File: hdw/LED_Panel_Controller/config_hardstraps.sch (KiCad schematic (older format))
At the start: 0 parts

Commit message: lots of schematic progress
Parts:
- added R? (x2): 10k, Resistors_SMD:R_0402, symbol Custom_Library:R_Custom
- added R? (x2): 10, Resistors_SMD:R_0402, symbol Custom_Library:R_Custom
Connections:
- new net +3V3: R?.1, R?.1
- new net GND: R?.2, R?.2
- new net ~ETC_Config: R?.1, R?.2
- new net ~Telemetry_Config: R?.1, R?.2
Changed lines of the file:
@@
 encoding utf-8
 Sheet 12 34
-Title ""
-Date "2020-09-08"
-Rev ""
-Comp ""
+Title "LED Panel Controller"
+Date "2020-12-23"
+Rev "A"
+Comp "Drew Maatman, Logan Wedel"
 Comment1 ""
 Comment2 ""
@@
 Comment4 ""
 $EndDescr
+$Comp
+L Custom_Library:R_Custom R?
+U 1 1 5FFD2F97
+P 2880 2230
+AR Path="/5D6B2673/5FFD2F97" Ref="R?"  Part="1"
+AR Path="/5D6C0D23/5FFD2F97" Ref="R?"  Part="1"
+AR Path="/5D77A516/5FFD2F97" Ref="R?"  Part="1"
+AR Path="/5E939CFF/5FFD2F97" Ref="R?"  Part="1"
+AR Path="/5F581B41/5FFD2F97" Ref="R?"  Part="1"
+AR Path="/5F5829EF/5FFD2F97" Ref="R?"  Part="1"
+F 0 "R?" H 2790 2230 50  0000 R CNN
+F 1 "10k" V 2880 2160 50  0000 L CNN
+F 2 "Resistors_SMD:R_0402" H 2880 2230 50  0001 C CNN
+F 3 "" H 2880 2230 50  0001 C CNN
+F 4 "0402" H 2980 2300 50  0000 L CNN "display_footprint"
+F 5 "1%" H 2980 2200 50  0000 L CNN "Tolerance"
+F 6 "1/16W" H 2980 2100 50  0000 L CNN "Wattage"
+F 7 "" H 3180 2630 60  0001 C CNN "Digi-Key PN"
+	1    2880 2230
+	-1   0    0    -1
+$EndComp
+$Comp
+L Custom_Library:R_Custom R?
+U 1 1 5FFD2FCD
+P 2880 2690
+AR Path="/5D6B2673/5FFD2FCD" Ref="R?"  Part="1"
+AR Path="/5D6C0D23/5FFD2FCD" Ref="R?"  Part="1"
+AR Path="/5D77A516/5FFD2FCD" Ref="R?"  Part="1"
+AR Path="/5E939CFF/5FFD2FCD" Ref="R?"  Part="1"
+AR Path="/5F581B41/5FFD2FCD" Ref="R?"  Part="1"
+AR Path="/5F5829EF/5FFD2FCD" Ref="R?"  Part="1"
+F 0 "R?" H 2790 2690 50  0000 R CNN
+F 1 "10" V 2880 2640 50  0000 L CNN
+F 2 "Resistors_SMD:R_0402" H 2880 2690 50  0001 C CNN
+F 3 "" H 2880 2690 50  0001 C CNN
+F 4 "0402" H 2980 2760 50  0000 L CNN "display_footprint"
+F 5 "1%" H 2980 2660 50  0000 L CNN "Tolerance"
+F 6 "1/16W" H 2980 2560 50  0000 L CNN "Wattage"
+F 7 "Telemetry" H 2610 2600 50  0000 C CNN "Configuration"
+	1    2880 2690
+	-1   0    0    -1
+$EndComp
+$Comp
+L power:GND #PWR?
+U 1 1 5FFD37BE
+P 2880 2840
+F 0 "#PWR?" H 2880 2590 50  0001 C CNN
+F 1 "GND" H 2880 2690 50  0000 C CNN
+F 2 "" H 2880 2840 50  0001 C CNN
+F 3 "" H 2880 2840 50  0001 C CNN
+	1    2880 2840
+	1    0    0    -1
+$EndComp
+$Comp
+L power:+3.3V #PWR?
+U 1 1 5FFD3948
+P 2880 2080
+F 0 "#PWR?" H 2880 1930 50  0001 C CNN
+F 1 "+3.3V" H 2880 2220 50  0000 C CNN
+F 2 "" H 2880 2080 50  0001 C CNN
+F 3 "" H 2880 2080 50  0001 C CNN
+	1    2880 2080
+	1    0    0    -1
+$EndComp
+Wire Wire Line
+	2880 2540 2880 2460
+Text GLabel 2960 2460 2    50   Output ~ 0
+~Telemetry_Config
+Wire Wire Line
+	2960 2460 2880 2460
+Connection ~ 2880 2460
+Wire Wire Line
+	2880 2460 2880 2380
+$Comp
+L Custom_Library:R_Custom R?
+U 1 1 5FFD5206
+P 4440 2230
+AR Path="/5D6B2673/5FFD5206" Ref="R?"  Part="1"
+AR Path="/5D6C0D23/5FFD5206" Ref="R?"  Part="1"
+AR Path="/5D77A516/5FFD5206" Ref="R?"  Part="1"
+AR Path="/5E939CFF/5FFD5206" Ref="R?"  Part="1"
+AR Path="/5F581B41/5FFD5206" Ref="R?"  Part="1"
+AR Path="/5F5829EF/5FFD5206" Ref="R?"  Part="1"
+F 0 "R?" H 4350 2230 50  0000 R CNN
+F 1 "10k" V 4440 2160 50  0000 L CNN
+F 2 "Resistors_SMD:R_0402" H 4440 2230 50  0001 C CNN
+F 3 "" H 4440 2230 50  0001 C CNN
+F 4 "0402" H 4540 2300 50  0000 L CNN "display_footprint"
+F 5 "1%" H 4540 2200 50  0000 L CNN "Tolerance"
+F 6 "1/16W" H 4540 2100 50  0000 L CNN "Wattage"
+F 7 "" H 4740 2630 60  0001 C CNN "Digi-Key PN"
+	1    4440 2230
+	-1   0    0    -1
+$EndComp
+$Comp
+L Custom_Library:R_Custom R?
+U 1 1 5FFD525E
+P 4440 2690
+AR Path="/5D6B2673/5FFD525E" Ref="R?"  Part="1"
+AR Path="/5D6C0D23/5FFD525E" Ref="R?"  Part="1"
+AR Path="/5D77A516/5FFD525E" Ref="R?"  Part="1"
+AR Path="/5E939CFF/5FFD525E" Ref="R?"  Part="1"
+AR Path="/5F581B41/5FFD525E" Ref="R?"  Part="1"
+AR Path="/5F5829EF/5FFD525E" Ref="R?"  Part="1"
+F 0 "R?" H 4350 2690 50  0000 R CNN
+F 1 "10" V 4440 2640 50  0000 L CNN
+F 2 "Resistors_SMD:R_0402" H 4440 2690 50  0001 C CNN
+F 3 "" H 4440 2690 50  0001 C CNN
+F 4 "0402" H 4540 2760 50  0000 L CNN "display_footprint"
+F 5 "1%" H 4540 2660 50  0000 L CNN "Tolerance"
+F 6 "1/16W" H 4540 2560 50  0000 L CNN "Wattage"
+F 7 "ETC" H 4280 2600 50  0000 C CNN "Configuration"
+	1    4440 2690
+	-1   0    0    -1
+$EndComp
+$Comp
+L power:GND #PWR?
+U 1 1 5FFD5268
+P 4440 2840
+F 0 "#PWR?" H 4440 2590 50  0001 C CNN
+F 1 "GND" H 4440 2690 50  0000 C CNN
+F 2 "" H 4440 2840 50  0001 C CNN
+F 3 "" H 4440 2840 50  0001 C CNN
+	1    4440 2840
+	1    0    0    -1
+$EndComp
+$Comp
+L power:+3.3V #PWR?
+U 1 1 5FFD5272
+P 4440 2080
+F 0 "#PWR?" H 4440 1930 50  0001 C CNN
+F 1 "+3.3V" H 4440 2220 50  0000 C CNN
+F 2 "" H 4440 2080 50  0001 C CNN
+F 3 "" H 4440 2080 50  0001 C CNN
+	1    4440 2080
+	1    0    0    -1
+$EndComp
+Wire Wire Line
+	4440 2540 4440 2460
+Text GLabel 4520 2460 2    50   Output ~ 0
+~ETC_Config
+Wire Wire Line
+	4520 2460 4440 2460
+Connection ~ 4440 2460
+Wire Wire Line
+	4440 2460 4440 2380
 $EndSCHEMATC

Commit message: made a lot more schematic progress
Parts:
- added R? (x3): 10k, Resistors_SMD:R_0402, symbol Custom_Library:R_Custom
- added R? (x3): 10, Resistors_SMD:R_0402, symbol Custom_Library:R_Custom
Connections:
- net +3V3: now also R?.1, R?.1, R?.1
- net GND: now also R?.2, R?.2, R?.2
- new net ~BACKUP_RTC_Config: R?.1, R?.2
- new net ~SPI_FLASH_Config: R?.1, R?.2
- new net ~WIFI_Config: R?.1, R?.2
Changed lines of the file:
@@
 Wire Wire Line
 	4440 2460 4440 2380
+$Comp
+L Custom_Library:R_Custom R?
+U 1 1 601F5320
+P 6000 2230
+AR Path="/5D6B2673/601F5320" Ref="R?"  Part="1"
+AR Path="/5D6C0D23/601F5320" Ref="R?"  Part="1"
+AR Path="/5D77A516/601F5320" Ref="R?"  Part="1"
+AR Path="/5E939CFF/601F5320" Ref="R?"  Part="1"
+AR Path="/5F581B41/601F5320" Ref="R?"  Part="1"
+AR Path="/5F5829EF/601F5320" Ref="R?"  Part="1"
+F 0 "R?" H 5910 2230 50  0000 R CNN
+F 1 "10k" V 6000 2160 50  0000 L CNN
+F 2 "Resistors_SMD:R_0402" H 6000 2230 50  0001 C CNN
+F 3 "" H 6000 2230 50  0001 C CNN
+F 4 "0402" H 6100 2300 50  0000 L CNN "display_footprint"
+F 5 "1%" H 6100 2200 50  0000 L CNN "Tolerance"
+F 6 "1/16W" H 6100 2100 50  0000 L CNN "Wattage"
+F 7 "" H 6300 2630 60  0001 C CNN "Digi-Key PN"
+	1    6000 2230
+	-1   0    0    -1
+$EndComp
+$Comp
+L Custom_Library:R_Custom R?
+U 1 1 601F53B6
+P 6000 2690
+AR Path="/5D6B2673/601F53B6" Ref="R?"  Part="1"
+AR Path="/5D6C0D23/601F53B6" Ref="R?"  Part="1"
+AR Path="/5D77A516/601F53B6" Ref="R?"  Part="1"
+AR Path="/5E939CFF/601F53B6" Ref="R?"  Part="1"
+AR Path="/5F581B41/601F53B6" Ref="R?"  Part="1"
+AR Path="/5F5829EF/601F53B6" Ref="R?"  Part="1"
+F 0 "R?" H 5910 2690 50  0000 R CNN
+F 1 "10" V 6000 2640 50  0000 L CNN
+F 2 "Resistors_SMD:R_0402" H 6000 2690 50  0001 C CNN
+F 3 "" H 6000 2690 50  0001 C CNN
+F 4 "0402" H 6100 2760 50  0000 L CNN "display_footprint"
+F 5 "1%" H 6100 2660 50  0000 L CNN "Tolerance"
+F 6 "1/16W" H 6100 2560 50  0000 L CNN "Wattage"
+F 7 "WIFI" H 5840 2600 50  0000 C CNN "Configuration"
+	1    6000 2690
+	-1   0    0    -1
+$EndComp
+$Comp
+L power:GND #PWR?
+U 1 1 601F53C0
+P 6000 2840
+F 0 "#PWR?" H 6000 2590 50  0001 C CNN
+F 1 "GND" H 6000 2690 50  0000 C CNN
+F 2 "" H 6000 2840 50  0001 C CNN
+F 3 "" H 6000 2840 50  0001 C CNN
+	1    6000 2840
+	1    0    0    -1
+$EndComp
+$Comp
+L power:+3.3V #PWR?
+U 1 1 601F53CA
+P 6000 2080
+F 0 "#PWR?" H 6000 1930 50  0001 C CNN
+F 1 "+3.3V" H 6000 2220 50  0000 C CNN
+F 2 "" H 6000 2080 50  0001 C CNN
+F 3 "" H 6000 2080 50  0001 C CNN
+	1    6000 2080
+	1    0    0    -1
+$EndComp
+Wire Wire Line
+	6000 2540 6000 2460
+Text GLabel 6080 2460 2    50   Output ~ 0
+~WIFI_Config
+Wire Wire Line
+	6080 2460 6000 2460
+Connection ~ 6000 2460
+Wire Wire Line
+	6000 2460 6000 2380
+$Comp
+L Custom_Library:R_Custom R?
+U 1 1 6025A56C
+P 7250 2230
+AR Path="/5D6B2673/6025A56C" Ref="R?"  Part="1"
+AR Path="/5D6C0D23/6025A56C" Ref="R?"  Part="1"
+AR Path="/5D77A516/6025A56C" Ref="R?"  Part="1"
+AR Path="/5E939CFF/6025A56C" Ref="R?"  Part="1"
+AR Path="/5F581B41/6025A56C" Ref="R?"  Part="1"
+AR Path="/5F5829EF/6025A56C" Ref="R?"  Part="1"
+F 0 "R?" H 7160 2230 50  0000 R CNN
+F 1 "10k" V 7250 2160 50  0000 L CNN
+F 2 "Resistors_SMD:R_0402" H 7250 2230 50  0001 C CNN
+F 3 "" H 7250 2230 50  0001 C CNN
+F 4 "0402" H 7350 2300 50  0000 L CNN "display_footprint"
+F 5 "1%" H 7350 2200 50  0000 L CNN "Tolerance"
+F 6 "1/16W" H 7350 2100 50  0000 L CNN "Wattage"
+F 7 "" H 7550 2630 60  0001 C CNN "Digi-Key PN"
+	1    7250 2230
+	-1   0    0    -1
+$EndComp
+$Comp
+L Custom_Library:R_Custom R?
+U 1 1 6025A640
+P 7250 2690
+AR Path="/5D6B2673/6025A640" Ref="R?"  Part="1"
+AR Path="/5D6C0D23/6025A640" Ref="R?"  Part="1"
+AR Path="/5D77A516/6025A640" Ref="R?"  Part="1"
+AR Path="/5E939CFF/6025A640" Ref="R?"  Part="1"
+AR Path="/5F581B41/6025A640" Ref="R?"  Part="1"
+AR Path="/5F5829EF/6025A640" Ref="R?"  Part="1"
+F 0 "R?" H 7160 2690 50  0000 R CNN
+F 1 "10" V 7250 2640 50  0000 L CNN
+F 2 "Resistors_SMD:R_0402" H 7250 2690 50  0001 C CNN
+F 3 "" H 7250 2690 50  0001 C CNN
+F 4 "0402" H 7350 2760 50  0000 L CNN "display_footprint"
+F 5 "1%" H 7350 2660 50  0000 L CNN "Tolerance"
+F 6 "1/16W" H 7350 2560 50  0000 L CNN "Wattage"
+F 7 "BACKUP_RTC" H 7160 2600 50  0000 R CNN "Configuration"
+	1    7250 2690
+	-1   0    0    -1
+$EndComp
+$Comp
+L power:GND #PWR?
+U 1 1 6025A64A
+P 7250 2840
+F 0 "#PWR?" H 7250 2590 50  0001 C CNN
+F 1 "GND" H 7250 2690 50  0000 C CNN
+F 2 "" H 7250 2840 50  0001 C CNN
+F 3 "" H 7250 2840 50  0001 C CNN
+	1    7250 2840
+	1    0    0    -1
+$EndComp
+$Comp
+L power:+3.3V #PWR?
+U 1 1 6025A654
+P 7250 2080
+F 0 "#PWR?" H 7250 1930 50  0001 C CNN
+F 1 "+3.3V" H 7250 2220 50  0000 C CNN
+F 2 "" H 7250 2080 50  0001 C CNN
+F 3 "" H 7250 2080 50  0001 C CNN
+	1    7250 2080
+	1    0    0    -1
+$EndComp
+Wire Wire Line
+	7250 2540 7250 2460
+Text GLabel 7330 2460 2    50   Output ~ 0
+~BACKUP_RTC_Config
+Wire Wire Line
+	7330 2460 7250 2460
+Connection ~ 7250 2460
+Wire Wire Line
+	7250 2460 7250 2380
+$Comp
+L Custom_Library:R_Custom R?
+U 1 1 6026E7E6
+P 2880 3440
+AR Path="/5D6B2673/6026E7E6" Ref="R?"  Part="1"
+AR Path="/5D6C0D23/6026E7E6" Ref="R?"  Part="1"
+AR Path="/5D77A516/6026E7E6" Ref="R?"  Part="1"
+AR Path="/5E939CFF/6026E7E6" Ref="R?"  Part="1"
+AR Path="/5F581B41/6026E7E6" Ref="R?"  Part="1"
+AR Path="/5F5829EF/6026E7E6" Ref="R?"  Part="1"
+F 0 "R?" H 2790 3440 50  0000 R CNN
+F 1 "10k" V 2880 3370 50  0000 L CNN
+F 2 "Resistors_SMD:R_0402" H 2880 3440 50  0001 C CNN
+F 3 "" H 2880 3440 50  0001 C CNN
+F 4 "0402" H 2980 3510 50  0000 L CNN "display_footprint"
+F 5 "1%" H 2980 3410 50  0000 L CNN "Tolerance"
+F 6 "1/16W" H 2980 3310 50  0000 L CNN "Wattage"
+F 7 "" H 3180 3840 60  0001 C CNN "Digi-Key PN"
+	1    2880 3440
+	-1   0    0    -1
+$EndComp
+$Comp
+L Custom_Library:R_Custom R?
+U 1 1 6026E8F8
+P 2880 3900
+AR Path="/5D6B2673/6026E8F8" Ref="R?"  Part="1"
+AR Path="/5D6C0D23/6026E8F8" Ref="R?"  Part="1"
+AR Path="/5D77A516/6026E8F8" Ref="R?"  Part="1"
+AR Path="/5E939CFF/6026E8F8" Ref="R?"  Part="1"
+AR Path="/5F581B41/6026E8F8" Ref="R?"  Part="1"
+AR Path="/5F5829EF/6026E8F8" Ref="R?"  Part="1"
+F 0 "R?" H 2790 3900 50  0000 R CNN
+F 1 "10" V 2880 3850 50  0000 L CNN
+F 2 "Resistors_SMD:R_0402" H 2880 3900 50  0001 C CNN
+F 3 "" H 2880 3900 50  0001 C CNN
+F 4 "0402" H 2980 3970 50  0000 L CNN "display_footprint"
+F 5 "1%" H 2980 3870 50  0000 L CNN "Tolerance"
+F 6 "1/16W" H 2980 3770 50  0000 L CNN "Wattage"
+F 7 "SPI_FLASH" H 2610 3810 50  0000 C CNN "Configuration"
+	1    2880 3900
+	-1   0    0    -1
+$EndComp
+$Comp
+L power:GND #PWR?
+U 1 1 6026E902
+P 2880 4050
+F 0 "#PWR?" H 2880 3800 50  0001 C CNN
+F 1 "GND" H 2880 3900 50  0000 C CNN
+F 2 "" H 2880 4050 50  0001 C CNN
+F 3 "" H 2880 4050 50  0001 C CNN
+	1    2880 4050
+	1    0    0    -1
+$EndComp
+$Comp
+L power:+3.3V #PWR?
+U 1 1 6026E90C
+P 2880 3290
+F 0 "#PWR?" H 2880 3140 50  0001 C CNN
+F 1 "+3.3V" H 2880 3430 50  0000 C CNN
+F 2 "" H 2880 3290 50  0001 C CNN
+F 3 "" H 2880 3290 50  0001 C CNN
+	1    2880 3290
+	1    0    0    -1
+$EndComp
+Wire Wire Line
+	2880 3750 2880 3670
+Text GLabel 2960 3670 2    50   Output ~ 0
+~SPI_FLASH_Config
+Wire Wire Line
+	2960 3670 2880 3670
+Connection ~ 2880 3670
+Wire Wire Line
+	2880 3670 2880 3590
 $EndSCHEMATC

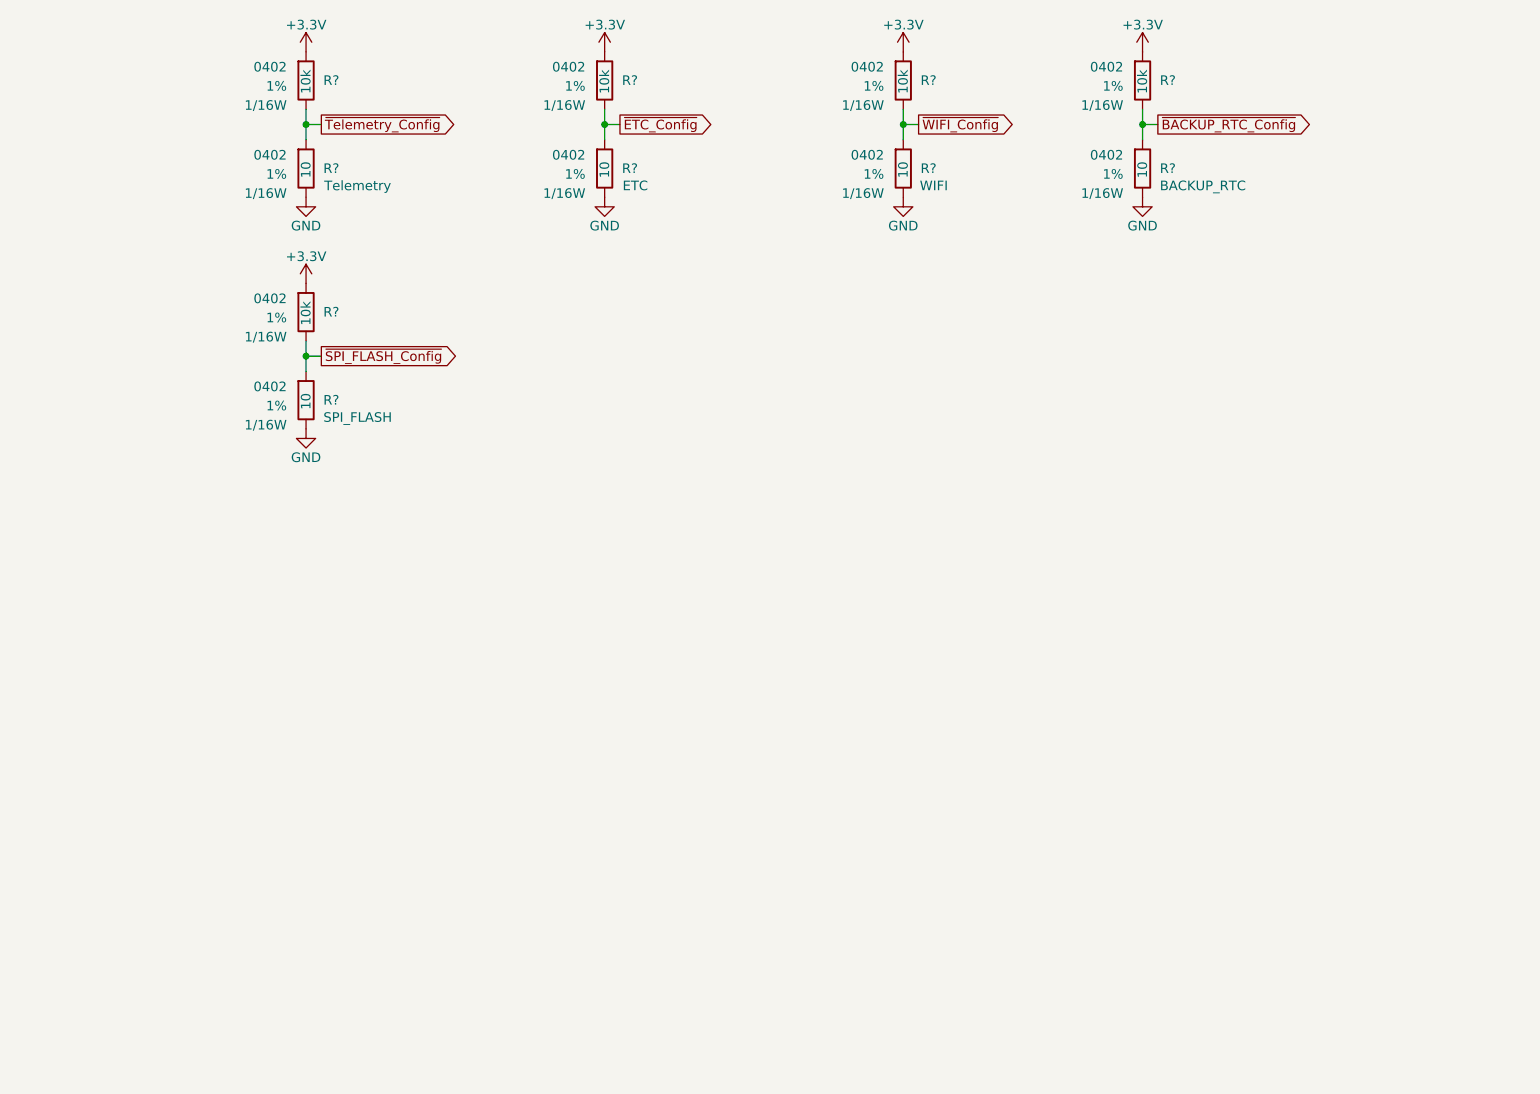
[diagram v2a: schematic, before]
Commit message: added some test points, ambient temp sensor
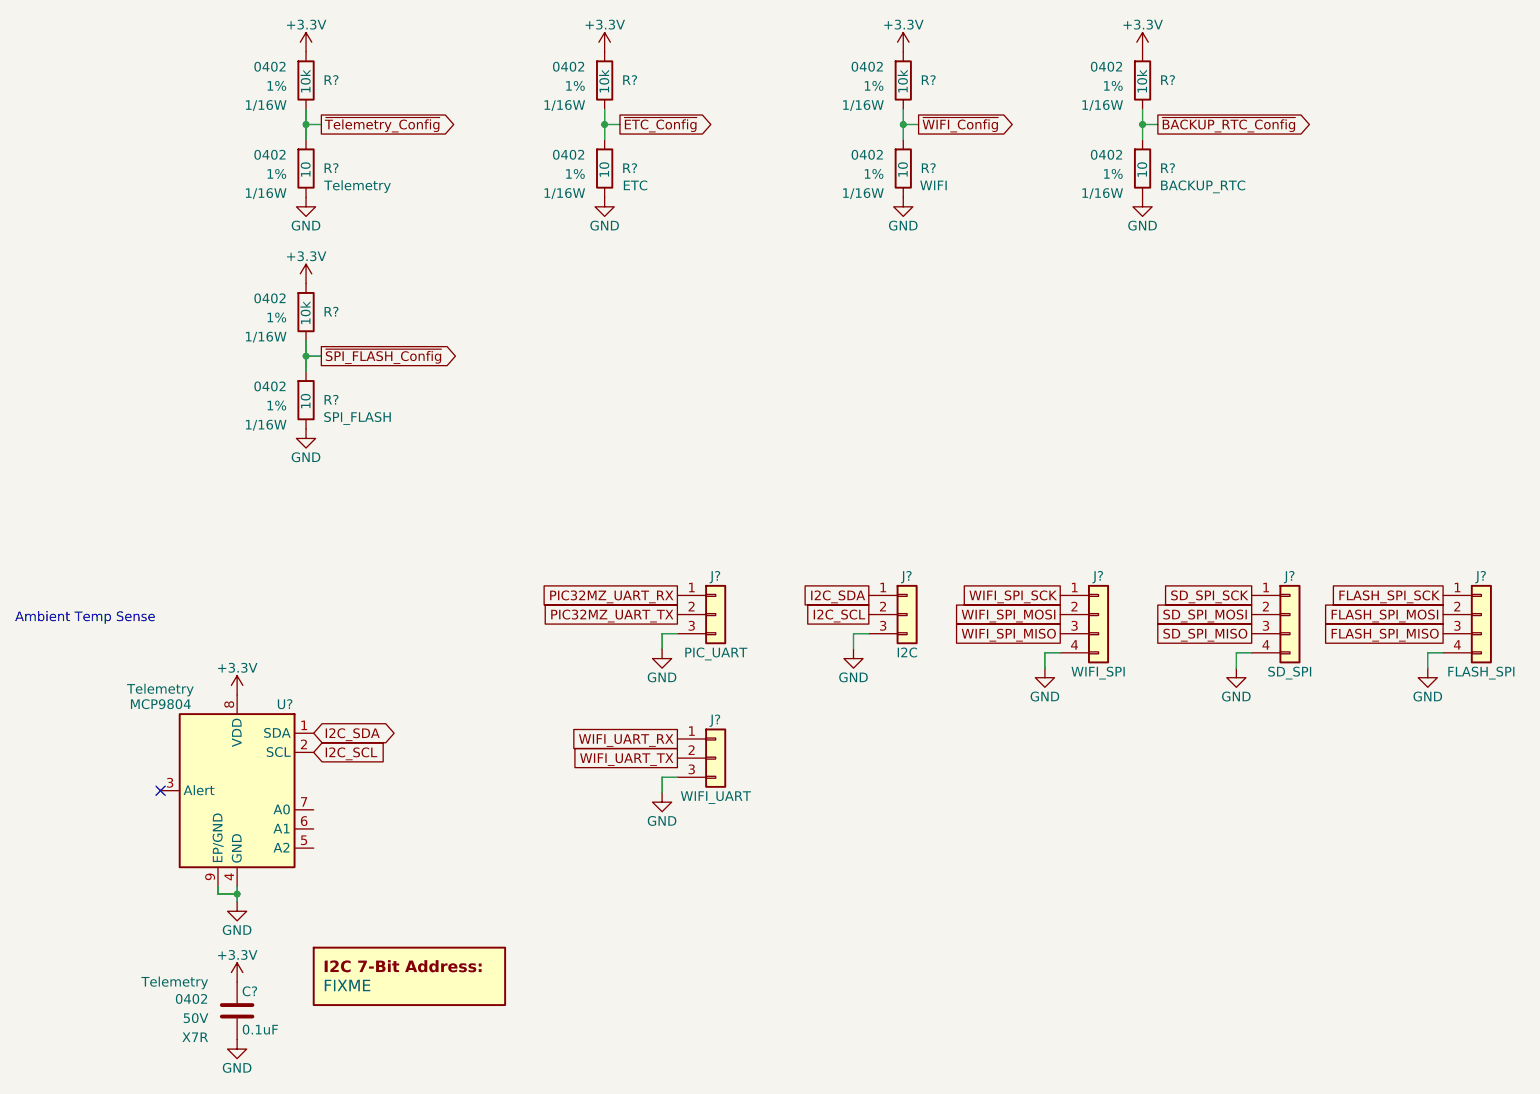
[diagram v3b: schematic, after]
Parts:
- added C?: 0.1uF, Capacitors_SMD:C_0402, symbol Custom_Library:C_Custom
- added DOC?: FIXME, symbol Custom_Library:I2C_Address
- added J?: I2C, symbol Connector_Generic:Conn_01x03
- added J?: WIFI_SPI, symbol Connector_Generic:Conn_01x04
- added J?: SD_SPI, symbol Connector_Generic:Conn_01x04
- added J?: FLASH_SPI, symbol Connector_Generic:Conn_01x04
- added J?: PIC_UART, symbol Connector_Generic:Conn_01x03
- added J?: WIFI_UART, symbol Connector_Generic:Conn_01x03
- added U?: MCP9804, Package_DFN_QFN:DFN-8-1EP_3x2mm_P0.5mm_EP1.3x1.5mm, symbol Sensor_Temperature:MCP9804_DFN
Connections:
- net +3V3: now also C?.1, U?.8 (VDD)
- net GND: now also C?.2, J?.3 (Pin_3), J?.3 (Pin_3), J?.3 (Pin_3), J?.4 (Pin_4), J?.4 (Pin_4), J?.4 (Pin_4), U?.4 (GND), U?.9 (EP/GND)
- new net FLASH_SPI_MISO: J?.3 (Pin_3)
- new net FLASH_SPI_MOSI: J?.2 (Pin_2)
- new net FLASH_SPI_SCK: J?.1 (Pin_1)
- new net I2C_SCL: J?.2 (Pin_2), U?.2 (SCL)
- new net I2C_SDA: J?.1 (Pin_1), U?.1 (SDA)
- new net PIC32MZ_UART_RX: J?.1 (Pin_1)
- new net PIC32MZ_UART_TX: J?.2 (Pin_2)
- new net SD_SPI_MISO: J?.3 (Pin_3)
- new net SD_SPI_MOSI: J?.2 (Pin_2)
- new net SD_SPI_SCK: J?.1 (Pin_1)
- new net WIFI_SPI_MISO: J?.3 (Pin_3)
- new net WIFI_SPI_MOSI: J?.2 (Pin_2)
- new net WIFI_SPI_SCK: J?.1 (Pin_1)
- new net WIFI_UART_RX: J?.1 (Pin_1)
- new net WIFI_UART_TX: J?.2 (Pin_2)
- no-connect marks 0 -> 1
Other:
- note added: "Ambient Temp Sense"
